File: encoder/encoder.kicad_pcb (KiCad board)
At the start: 2 copper layers, 28 x 25 mm, 9 parts, among them J1 GS3, J2 GS3, SW1 Rotary_Encoder_Switch, U1 STM32F030F4Px, X1 I2C-6P, X2 SWD

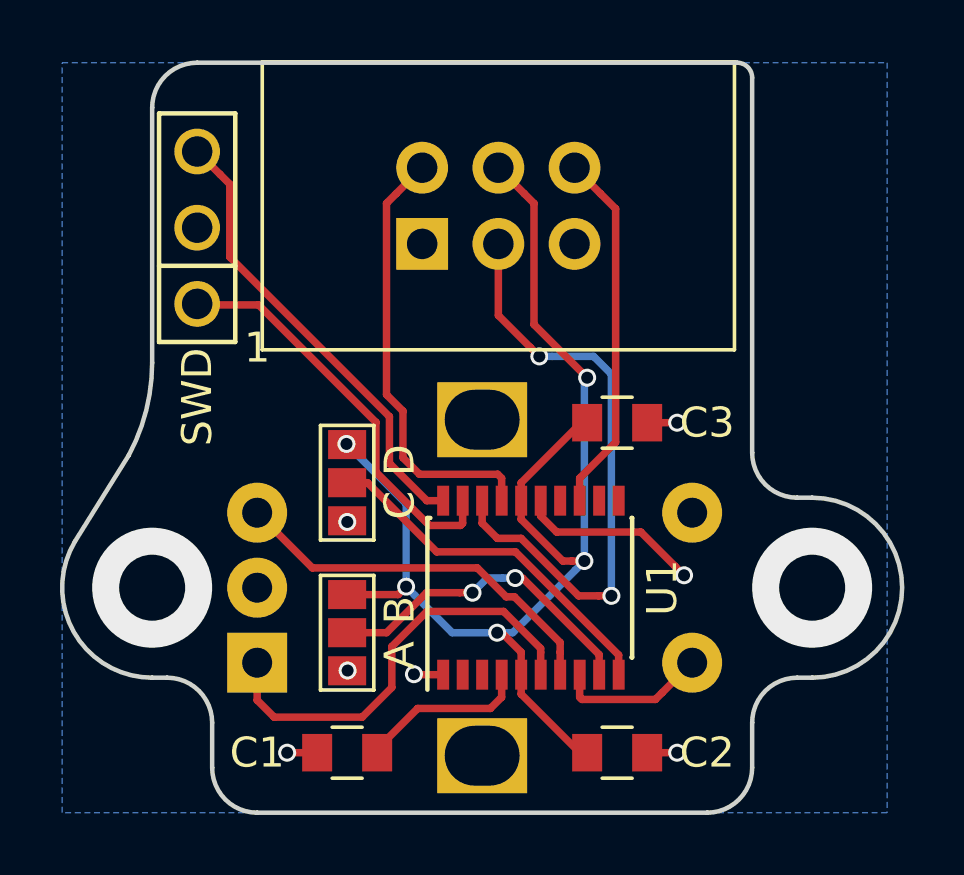
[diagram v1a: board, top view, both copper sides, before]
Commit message: Band switch support
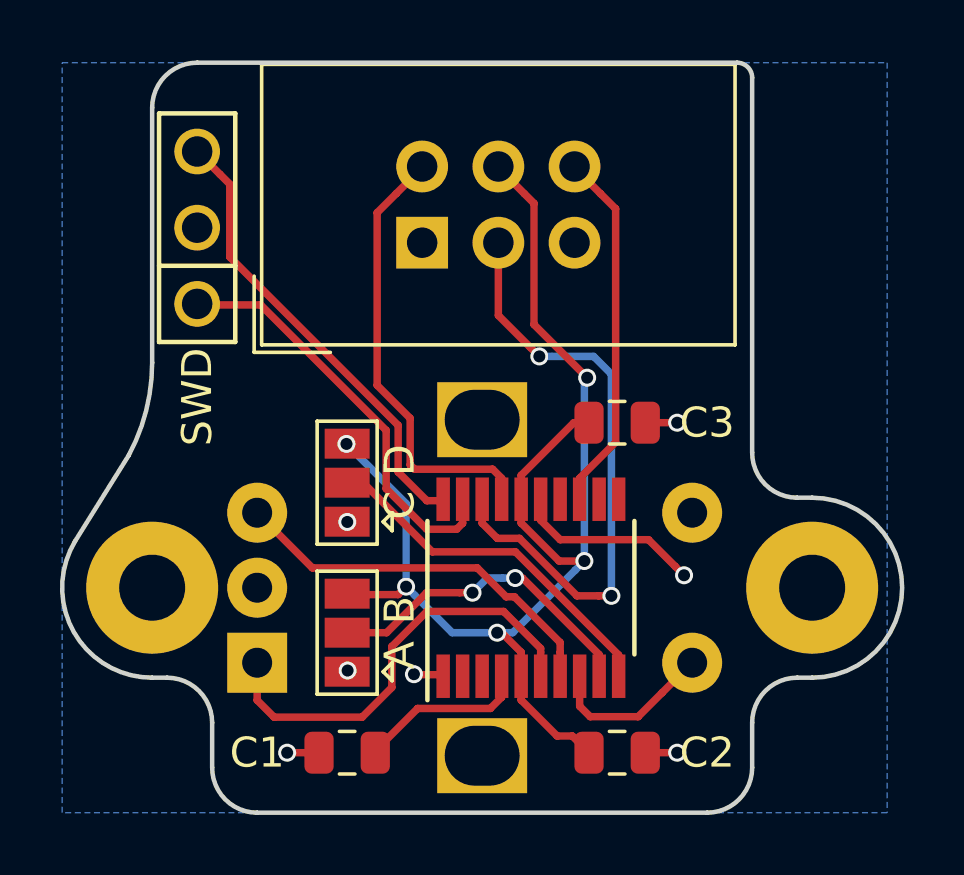
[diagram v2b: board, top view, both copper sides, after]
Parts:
- added H1: MountingHole_Pad, MountingHole:MountingHole_2.2mm_M2_Pad, F.Cu at (160.0, 109.0)
- added H2: MountingHole_Pad, MountingHole:MountingHole_2.2mm_M2_Pad, F.Cu at (182.0, 109.0)
- C1, C2, C3: footprint Capacitors_SMD:C_0805 -> Capacitor_SMD:C_0805_2012Metric
- J1, J2: footprint Connectors:GS3 -> Jumper:SolderJumper-3_P1.3mm_Open_Pad1.0x1.5mm
- SW1: footprint Rotary_Encoder:RotaryEncoder_Alps_EC12E-Switch_Vertical_H20mm -> device.farm:RotaryEncoder_Bourns_PEC12R-4x20F-Sxxxx
- U1: footprint Housings_SSOP:SSOP-20_4.4x6.5mm_Pitch0.65mm -> Package_SO:TSSOP-20_4.4x6.5mm_P0.65mm
- X1: footprint Connectors:IDC_Header_Straight_6pins -> Connector_IDC:IDC-Header_2x03_P2.54mm_Vertical
- turned X1 to 90 degrees
- turned J1 to 90 degrees
- turned J2 to 90 degrees
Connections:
- U1 pad 11: (no net) -> Net-(U1-Pad11)
- U1 pad 12: (no net) -> Net-(U1-Pad12)
- U1 pad 14: (no net) -> Net-(U1-Pad14)
- U1 pad 2: (no net) -> Net-(U1-Pad2)
- U1 pad 3: (no net) -> Net-(U1-Pad3)
- U1 pad 6: Net-(SW1-Pad1) -> Net-(SW1-PadA)
- U1 pad 7: Net-(SW1-Pad3) -> Net-(SW1-PadB)
- U1 pad 8: Net-(SW1-Pad4) -> Net-(SW1-PadS1)
- X1 pad 5: (no net) -> Net-(X1-Pad5)
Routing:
- net Net-(SW1-PadA): track 0.00 -> 14.6 mm
- net Net-(SW1-Pad1): track 14.6 -> 0.00 mm
- net Net-(SW1-PadB): track 0.00 -> 13.0 mm
- net Net-(SW1-Pad3): track 13.0 -> 0.00 mm
- net Net-(SW1-PadS1): track 0.00 -> 5.69 mm
- net Net-(SW1-Pad4): track 5.04 -> 0.00 mm
- net (no net): vias 2 -> 0
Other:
- net class Default: clearance 0.2 -> 0.15
- rule trace_clearance: 0.2 -> 0.15
